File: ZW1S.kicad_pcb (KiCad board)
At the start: 2 copper layers, 103.1 x 88.1 mm, 169 parts, among them J1 Conn_01x06_GH1.25, J10 Conn_01x04_GH1.25, J11 Conn_01x04_GH1.25, J12 Conn_01x04_GH1.25, J2 Conn_01x02_XH2.54, J3 Conn_01x02_XH2.54, J4 Conn_01x02_XH2.54, J5 Conn_01x02_XH2.54, J6 KF2EDGR-3.81-2P, J7 Conn_01x04_GH1.25, J8 KF2EDGR-3.81-2P, J9 KF2EDGR-3.81-2P, Q1 SI2306A, Q2 SI2306A, Q3 SI2306A, Q4 SI2306A, SW1 RST, U1 XC6206PxxxMR, U10 CH334P, U11 CH343P, U12 SW3526, U2 AT32F425K8U7-4, U3 TJA1044GTK/3Z, U4 TPS54302, U5 SCT2450, U6 XC6206PxxxMR, U7 CH397A, U8 XC6206PxxxMR, U9 CH343P, Y1 16MHz, Y2 25MHz, Y3 12MHz

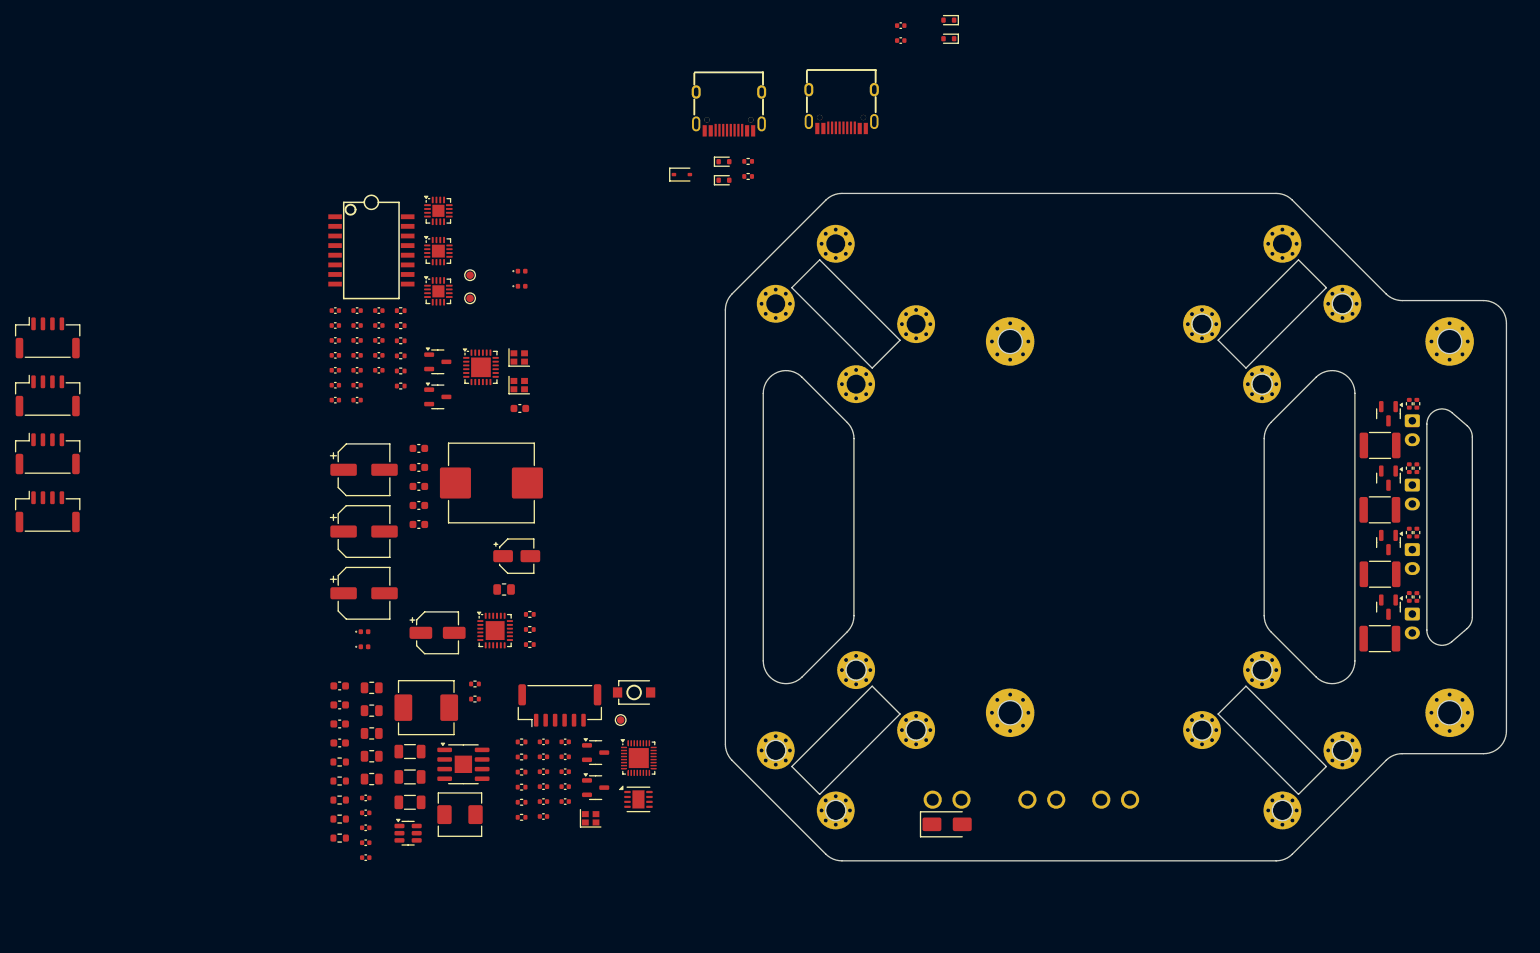
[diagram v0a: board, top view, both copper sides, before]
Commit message: 暂存: 布局布线基本完成(DRC未过，GND不全)
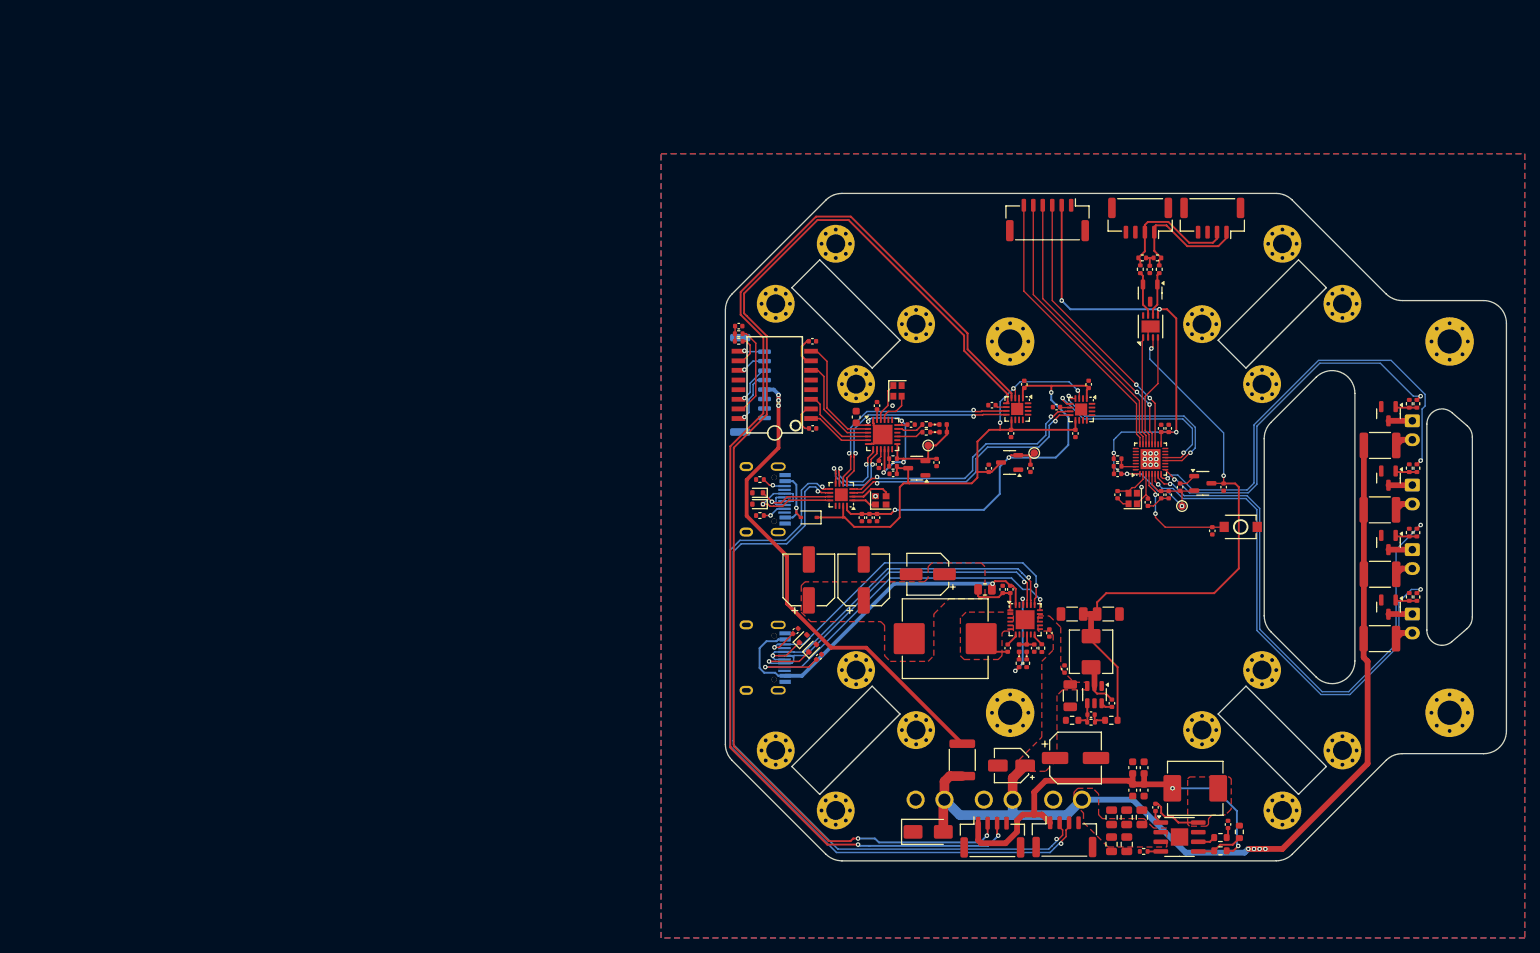
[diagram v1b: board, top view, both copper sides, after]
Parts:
- added F5: 24V@1.5A, Fuse:Fuse_1812_4532Metric, F.Cu at (160.2, 112.5)
- added J13: Conn_01x08_GH1.25, Connector_JST:JST_GH_SM08B-GHS-TB_1x08-1MP_P1.25mm_Horizontal, B.Cu at (132.3, 63.0)
- C52: renamed from C53; footprint Capacitor_SMD:C_0603_1608Metric -> Capacitor_SMD:C_0402_1005Metric
- C54: renamed from C55; footprint Capacitor_SMD:C_0603_1608Metric -> Capacitor_SMD:C_0402_1005Metric
- C55: renamed from C56; footprint Capacitor_SMD:C_0603_1608Metric -> Capacitor_SMD:C_0402_1005Metric
- C56: renamed from C57; footprint Capacitor_SMD:C_0603_1608Metric -> Capacitor_SMD:C_0402_1005Metric
- C57: renamed from C58; footprint Capacitor_SMD:C_0603_1608Metric -> Capacitor_SMD:C_0402_1005Metric
- D11: value SMAJ24CA -> SMAJ28CA
- USB1, USB2: moved to B.Cu
- moved J11 156.8 mm to (193.2, 41.0), turned to 180 degrees
- moved J12 149.3 mm to (183.7, 41.0), turned to 180 degrees
- moved J10 146.3 mm to (173.7, 122.7)
- moved J7 141.0 mm to (164.2, 122.7)
- moved R13 118.7 mm to (196.8, 122.0), turned to -90 degrees
- moved R7 116.7 mm to (194.3, 122.8), turned to 180 degrees
- moved R12 116.3 mm to (194.3, 124.5)
- moved C14 113.9 mm to (195.3, 121.0), turned to 90 degrees
- moved R3 110.5 mm to (186.0, 46.2), turned to 180 degrees
- moved R4 110.3 mm to (184.0, 46.2), turned to 180 degrees
- moved R5 107.2 mm to (186.2, 47.8), turned to -90 degrees
- moved C16 106.8 mm to (184.2, 116.5), turned to -90 degrees
- moved R6 106.5 mm to (183.8, 47.8), turned to -90 degrees
- moved C19 106.2 mm to (184.2, 113.5), turned to 90 degrees
- moved C11 105.6 mm to (182.8, 116.5), turned to -90 degrees
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- renumbered C11 to C10, C12 to C11, C13 to C12, C14 to C13, C15 to C14, C16 to C15, C17 to C16, C18 to C17, C19 to C18, C20 to C19, C21 to C20, C22 to C21, C23 to C22, C24 to C23, C25 to C24, C26 to C25, C27 to C26, C28 to C27, C29 to C28, C30 to C29, C31 to C30, C32 to C31, C33 to C32, C34 to C33, C35 to C34, C36 to C35, C37 to C36, C38 to C37, C39 to C38, C40 to C39, C41 to C40, C42 to C41, C43 to C42, C44 to C43, C45 to C44, C46 to C45, C47 to C46, C48 to C47, C49 to C48, C50 to C49, C6 to C5, C51 to C50, C52 to C51, C54 to C53, C59 to C58, C60 to C59, C7 to C6, C8 to C7, C9 to C8, C10 to C9, R5 to R3, R6 to R4, R3 to R5, R4 to R6
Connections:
- D1 pad 1: /mcu/CANH_IN -> /mcu/CANL_IN
- D1 pad 2: /mcu/CANL_IN -> /mcu/CANH_IN
- D4 pad 1: /usb/USB_DN -> /usb/USB_HUB_DN
- D5 pad 1: /usb/USB_DP -> /usb/USB_HUB_DP
- L3 pad 11: /usb/MID360_TXN -> MID360_TXN
- L3 pad 14: /usb/MID360_RXP -> MID360_RXP
- L3 pad 16: /usb/MID360_RXN -> MID360_RXN
- L3 pad 9: /usb/MID360_TXP -> MID360_TXP
- R28 pad 2: EXT_LED_1 -> EXT_LED_4
- R3 pad 1: /mcu/CANH_IN -> CANL
- R33 pad 2: EXT_LED_4 -> EXT_LED_1
- R4 pad 2: /mcu/CANL_IN -> CANH
- R5 pad 1: CANH -> CANL
- R5 pad 2: /mcu/CANH_IN -> /mcu/CANL_IN
- R6 pad 1: CANL -> CANH
- R6 pad 2: /mcu/CANL_IN -> /mcu/CANH_IN
- U12 pad 20: /power/VIN-5V0-SBC/DP -> /power/VIN-5V0-SBC/USB_DP
- U12 pad 21: /power/VIN-5V0-SBC/DN -> /power/VIN-5V0-SBC/USB_DN
- U2 pad 1: unconnected-(U2-VDD-Pad1) -> /mcu/3V3
- USB2 pad 5: /power/VIN-5V0-SBC/DN -> /power/VIN-5V0-SBC/USB_DN
- USB2 pad 6: /power/VIN-5V0-SBC/DP -> /power/VIN-5V0-SBC/USB_DP
- USB2 pad 7: /power/VIN-5V0-SBC/DN -> /power/VIN-5V0-SBC/USB_DN
- USB2 pad 8: /power/VIN-5V0-SBC/DP -> /power/VIN-5V0-SBC/USB_DP
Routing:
- net Lora_RX: track 0.00 -> 157.6 mm, vias 0 -> 2
- net Lora_TX: track 0.00 -> 154.6 mm, vias 0 -> 2
- net V_{power}: track 0.00 -> 126.7 mm, vias 0 -> 4
- net USB_4_DN: track 0.00 -> 99.0 mm, vias 0 -> 2
- net USB_4_DP: track 0.00 -> 96.8 mm, vias 0 -> 2
- net /mcu/3V3: track 0.00 -> 84.3 mm, vias 0 -> 6
- net 5V0_{assist}: track 0.00 -> 77.4 mm, vias 0 -> 2
- net /usb/VBUS: track 0.00 -> 75.6 mm, vias 0 -> 3
- net EXT_LED_2: track 0.00 -> 73.4 mm, vias 0 -> 2
- net Net-(J13-Pin_3): track 0.00 -> 67.1 mm, vias 0 -> 3
- net EXT_LED_1: track 0.00 -> 66.9 mm, vias 0 -> 2
- net /usb/3V3: track 0.00 -> 61.1 mm, vias 0 -> 3
- net EXT_LED_3: track 0.00 -> 59.4 mm, vias 0 -> 2
- net 5V0_{device}: track 0.00 -> 56.1 mm, vias 0 -> 2
- net /power/VIN-5V0-SBC/USB_DN: track 0.00 -> 51.3 mm, vias 0 -> 2
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- added copper zone on F.Cu, net /power/VIN-5V0-SBC/CSP
- added copper zone on B.Cu, net GND
- added copper zone on F.Cu, net GND
- added copper zone on F.Cu, net Net-(C54-Pad2)
- added copper zone on F.Cu, net Net-(U5-SW)
- added copper zone on F.Cu, net V_{power}
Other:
- outline, holes or cut-outs redrawn

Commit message: 提交生产: 2507271646
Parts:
- added G***: LOGO, LOGO, F.Cu at (172.0, 85.4)
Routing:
- net GND: track 16.2 -> 33.6 mm, vias 12 -> 175
- net /usb/3V3: track 61.1 -> 62.0 mm
- net 5V0_{device}: track 56.1 -> 56.6 mm
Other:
- board size 103.1 x 88.1 mm -> 99.6 x 88.1 mm
- board text added: "<-"
- board text added: "BIT-SGC"
- board text added: "C D R T V G"
- board text added: "CAN1-A"
- board text added: "CAN1-B"
- board text added: "DEBUG"
- board text added: "EXT_LED ->VBAT"
- board text added: "G x H L"
- board text added: "JLCJLCJLCJLC"
- board text added: "LOAR_{EXT}"
- board text added: "MID 360"
- board text added: "T+ T- R+ R- V V G G"
- board text added: "USB_{EXT}"
- board text added: "USB_{HUB}"
- board text added: "USB_{SBC_PWR}"
- board text added: "V + - G"
- board text added: "V T R G"
- board text added: "ZW1S Ver: 2507271646 SN:"

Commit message: fix: 修正TPS54302反馈电阻值
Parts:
- R11: value 49.9K -> 49.9R
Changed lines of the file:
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@@
 			)
 		)
-		(property "Value" "49.9K"
+		(property "Value" "49.9R"
 			(at 0 1.43 0)
 			(layer "F.Fab")

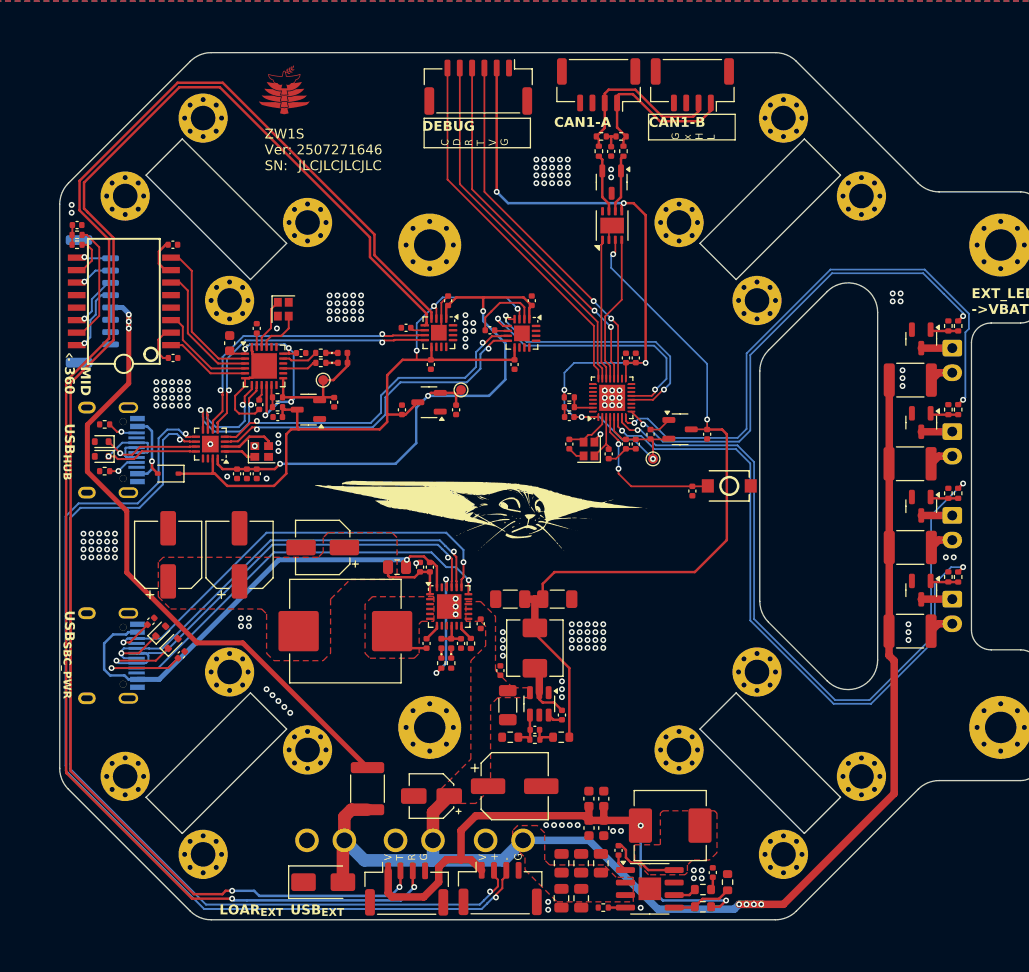
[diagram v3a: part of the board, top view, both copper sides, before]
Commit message: pref: USB外设改自供电，优化布线
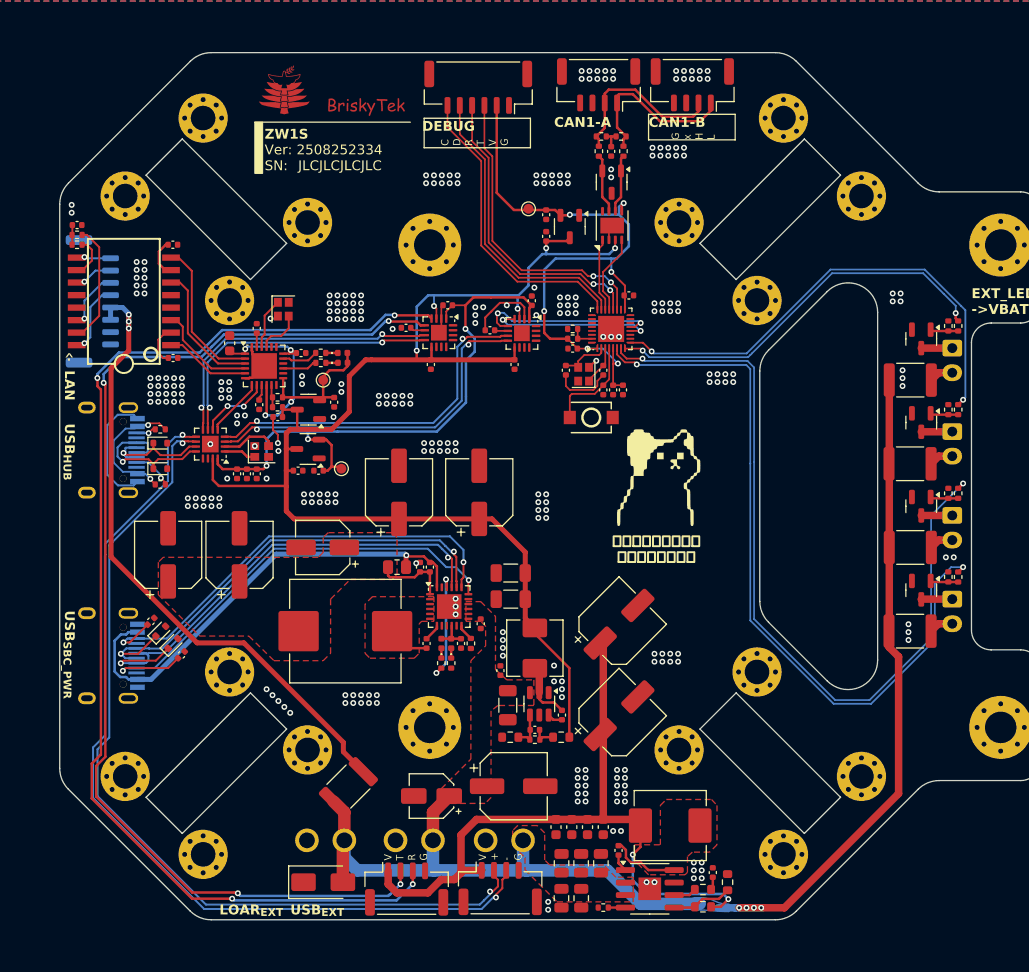
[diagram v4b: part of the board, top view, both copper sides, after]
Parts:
- removed the C5 at (187.5, 77.5)
- removed the D6 at (140.0, 80.5)
- added C14: 100uF/35V, Capacitor_SMD:CP_Elec_6.3x7.7, F.Cu at (185.8, 95.8)
- added C20: 100uF/35V, Capacitor_SMD:CP_Elec_6.3x7.7, F.Cu at (185.8, 105.1)
- added C22: 100uF/35V, Capacitor_SMD:CP_Elec_6.3x7.7, F.Cu at (163.4, 82.4)
- added C26: 100uF/35V, Capacitor_SMD:CP_Elec_6.3x7.7, F.Cu at (171.6, 82.4)
- J1: footprint Connector_JST:JST_GH_BM06B-GHS-TBT_1x06-1MP_P1.25mm_Vertical -> Connector_JST:JST_GH_SM06B-GHS-TB_1x06-1MP_P1.25mm_Horizontal
- R20, R21: value 5.1K -> 56K
- moved TP1 28.4 mm to (176.6, 53.6)
- moved C1 25.9 mm to (178.4, 56.4), turned to 90 degrees
- moved C7 24.7 mm to (178.4, 54.2), turned to -90 degrees
- moved U1 23.4 mm to (180.8, 55.4), turned to -90 degrees
- moved G*** 18.7 mm to (190.0, 80.4)
- moved SW1 15.6 mm to (183.0, 74.8)
- moved C45 15.3 mm to (155.3, 80.2), turned to 180 degrees
- moved TP3 14.5 mm to (157.6, 80.0)
- moved C6 13.7 mm to (184.2, 72.0)
- moved U8 13.2 mm to (154.2, 78.0)
- moved C41 12.2 mm to (153.2, 80.2), turned to 0 degrees
- moved C9 8.52 mm to (184.2, 70.0)
- moved R2 7.96 mm to (181.1, 65.8)
- moved Y1 7.62 mm to (182.2, 70.4)
- moved C8 7.51 mm to (180.4, 70.0)
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- renumbered C14 to C15, C15 to C16, C16 to C17, C17 to C18, C18 to C19, C19 to C21, C20 to C23, C21 to C24, C22 to C25, C23 to C27, C24 to C28, C25 to C29, C26 to C30, C27 to C31, C28 to C32, C29 to C33, C30 to C34, C31 to C35, C32 to C36, C33 to C37, C34 to C38, C35 to C39, C36 to C40, C37 to C41, C38 to C42, C39 to C43, C40 to C44, C41 to C45, C42 to C46, C43 to C47, C44 to C48, C45 to C49, C46 to C50, C47 to C51, C48 to C52, C49 to C53, C50 to C54, C51 to C55, C52 to C56, C53 to C57, C54 to C58, C55 to C59, C56 to C60, C57 to C61, C58 to C62, C59 to C63, D11 to D10, D7 to D6, D8 to D7, D9 to D8, D10 to D9
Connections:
- C35 pad 1: /usb/VBUS -> 5V0_{assist}
- C41 pad 1: /usb/VBUS -> 5V0_{assist}
- C44 pad 1: /usb/VBUS -> 5V0_{assist}
- C50 pad 1: /usb/VBUS -> 5V0_{assist}
- J1 pad MP: (no net) -> GND
- J10 pad MP: (no net) -> GND
- J11 pad MP: (no net) -> GND
- J12 pad MP: (no net) -> GND
- J13 pad MP: (no net) -> GND
- J7 pad MP: (no net) -> GND
- R15 pad 2: /usb/VBUS -> 5V0_{assist}
- R20 pad 1: GND -> /usb/VBUS
- R21 pad 1: GND -> /usb/VBUS
- R28 pad 2: EXT_LED_4 -> EXT_LED_3
- R29 pad 2: EXT_LED_3 -> EXT_LED_4
- U10 pad 15: /usb/VBUS -> 5V0_{assist}
- U11 pad 3: /usb/VBUS -> 5V0_{assist}
- U11 pad 7: /usb/USB_2_DP -> /usb/USB_3_DP
- U11 pad 8: /usb/USB_2_DN -> /usb/USB_3_DN
- U11 pad 9: /usb/VBUS -> 5V0_{assist}
- U6 pad 3: /usb/VBUS -> 5V0_{assist}
- U7 pad 7: /usb/USB_3_DN -> /usb/USB_2_DN
- U7 pad 8: /usb/USB_3_DP -> /usb/USB_2_DP
- U8 pad 3: /usb/VBUS -> 5V0_{assist}
- U9 pad 3: /usb/VBUS -> 5V0_{assist}
- U9 pad 9: /usb/VBUS -> 5V0_{assist}
- USB1 pad 11: /usb/VBUS_IN -> /usb/VBUS
- USB1 pad 2: /usb/VBUS_IN -> /usb/VBUS
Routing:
- net 5V0_{assist}: track 77.4 -> 156.2 mm, vias 2 -> 5
- net /usb/VBUS: track 75.6 -> 13.1 mm, vias 3 -> 2
- net Lora_TX: track 154.6 -> 115.3 mm, vias 2 -> 4
- net Lora_RX: track 157.6 -> 119.2 mm, vias 2 -> 4
- net /usb/USB_2_DN: track 28.8 -> 5.99 mm, vias 2 -> 0
- net /usb/USB_2_DP: track 29.6 -> 7.42 mm
- net /mcu/3V3: track 84.3 -> 65.1 mm
- net EXT_LED_3: track 59.4 -> 40.5 mm
- net /usb/USB_3_DN: track 11.6 -> 30.0 mm
- net /usb/USB_3_DP: track 13.1 -> 30.9 mm
- net 5V0_{device}: track 56.6 -> 71.6 mm
- net CTRL_RX: track 27.1 -> 16.8 mm
- net /usb/VBUS_IN: track 8.70 -> 0.00 mm, vias 1 -> 0
- net EXT_LED_2: track 73.4 -> 82.0 mm
- net EXT_LED_1: track 66.9 -> 75.3 mm
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- added copper zone on B.Cu, net V_{power}
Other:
- board text added: "LAN"
- board text added: "Ver: 2508252334 SN:"
- board text added: "ZW1S"
- board text added: "按道理我这个级别的 基米有权哈所有人"
- board text removed: "BIT-SGC"
- board text removed: "MID 360"
- board text removed: "ZW1S Ver: 2507271646 SN:"
